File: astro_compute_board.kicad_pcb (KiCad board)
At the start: 4 copper layers, 66.4 x 66.2 mm, 81 parts, among them J1 SWD, J10 ADC_IO, J2 I2C1, J6 USB_B_Micro, J8 RaspberryHeader, J9 VINPUT, Q1 QM6015D, Q2 IRF540S, Q3 IRF540S, SW1 SW_SPDT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

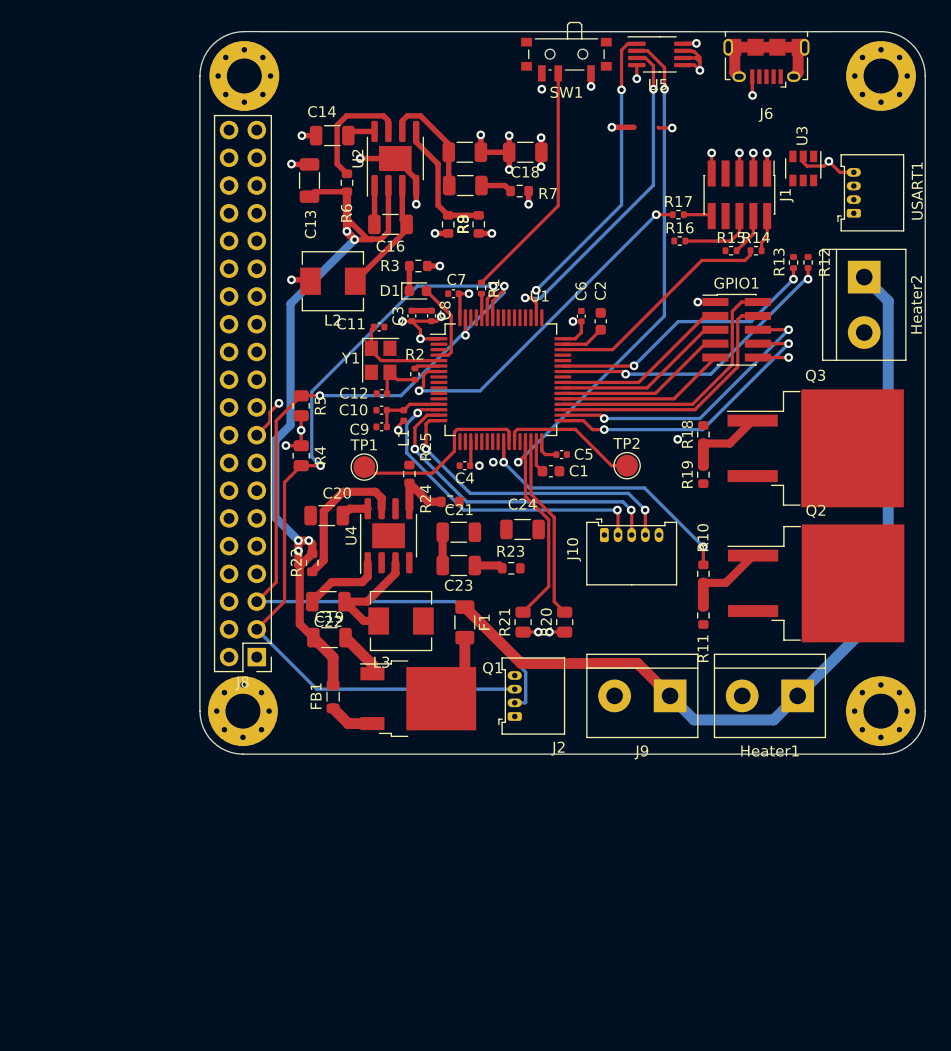
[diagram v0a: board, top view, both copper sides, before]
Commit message: JLCPCB Ready (but costly)
Contains many extender parts that make PCB expensive.
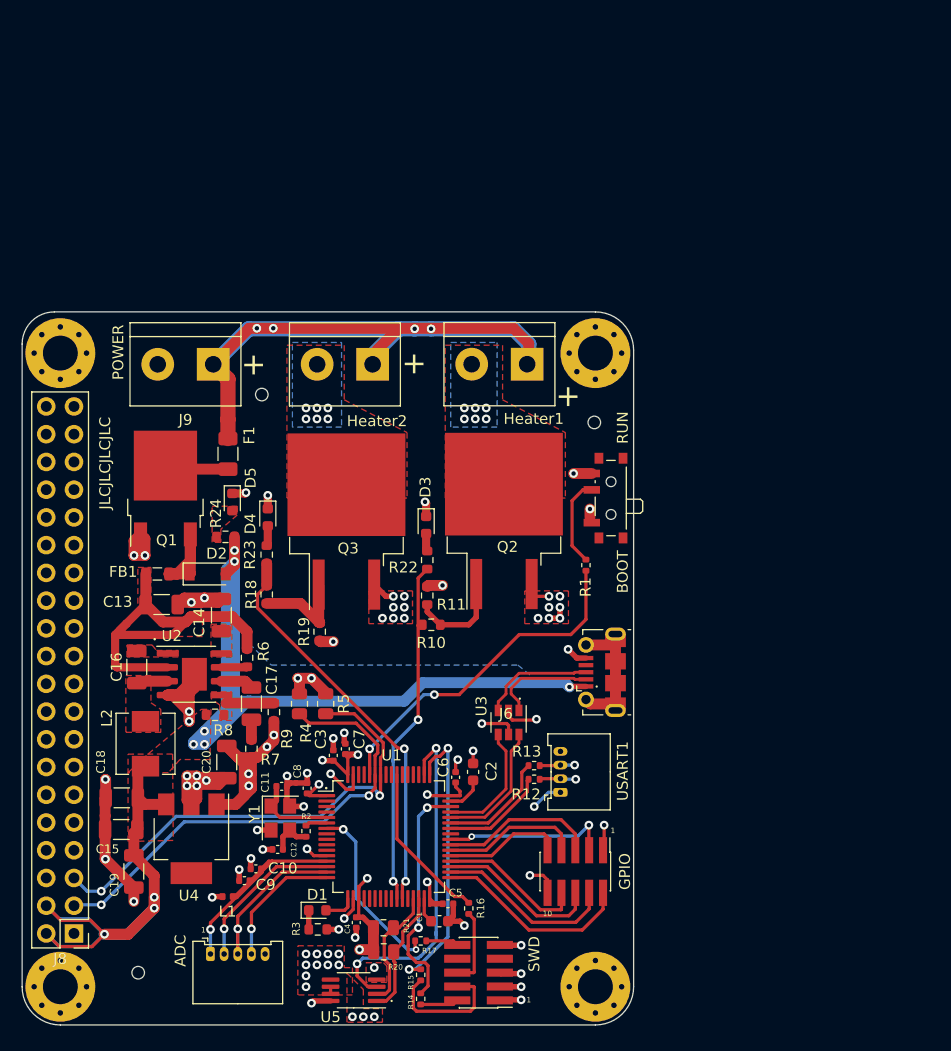
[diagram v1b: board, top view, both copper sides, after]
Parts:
- removed C21: Open, Capacitor_SMD:C_1206_3216Metric
- removed C22: 0.1u, Capacitor_SMD:C_1206_3216Metric
- removed C23: 2.2nF, Capacitor_SMD:C_1206_3216Metric
- removed C24: 22uF, Capacitor_SMD:C_1206_3216Metric
- removed GPIO1: GPIO_CONNECTOR, Connector_PinHeader_1.27mm:PinHeader_2x05_P1.27mm_Vertical_SMD
- removed J1: SWD, Connector_PinHeader_1.27mm:PinHeader_2x05_P1.27mm_Vertical_SMD
- removed J10: ADC_IO, Connector_Molex:Molex_PicoBlade_53048-0510_1x05_P1.25mm_Horizontal
- removed J2: I2C1, Connector_Molex:Molex_PicoBlade_53048-0410_1x04_P1.25mm_Horizontal
- removed L3: 6.8uH, Inductor_SMD:L_Sunlord_MWSA0518_5.4x5.2mm
- removed R25: 24k, Resistor_SMD:R_0603_1608Metric
- removed SW1: SW_SPDT, Button_Switch_SMD:SW_SPDT_PCM12
- removed TP1, TP2: TestPoint, TestPoint:TestPoint_Pad_D2.0mm
- added ADC: ADC_IO, Connector_Molex:Molex_PicoBlade_53048-0510_1x05_P1.25mm_Horizontal, F.Cu at (165.2, 151.7)
- added BOOT: SW_SPDT, Button_Switch_SMD:SW_SPDT_PCM12, F.Cu at (201.5, 109.9)
- added D2: B5817W-5819W, Diode_SMD:D_SOD-123, F.Cu at (164.9, 116.8)
- added D3: RED, LED_SMD:LED_0603_1608Metric, F.Cu at (184.9, 112.4)
- added D4: RED, LED_SMD:LED_0603_1608Metric, F.Cu at (170.4, 111.7)
- added D5: Green, LED_SMD:LED_0603_1608Metric, F.Cu at (167.2, 110.3)
- added GPIO: GPIO_CONNECTOR, Connector_PinHeader_1.27mm:PinHeader_2x05_P1.27mm_Vertical_SMD, F.Cu at (198.6, 144.1)
- added REF**: OSHW-Logo_11.4x12mm_SilkScreen, Symbol:OSHW-Logo_11.4x12mm_SilkScreen, B.Cu at (191.6, 110.5)
- added SWD: SWD, Connector_PinHeader_1.27mm:PinHeader_2x05_P1.27mm_Vertical_SMD, F.Cu at (189.7, 153.4)
- C15: value Open -> 22uF
- D1: value LED_Small -> BLUE
- J6: footprint Connector_USB:USB_Micro-B_Amphenol_10118194_Horizontal -> Connector_USB:USB_Micro-B_Molex-105017-0001
- R22: value 100k -> 1k
- R23: value 22k -> 1k
- R24: value 75k -> 1k
- R3: value 10k -> 2k
- R7: value 22k -> 33k
- R8: value 75k -> 62
- R9: value 24k -> 11.8
- U4: value RT7257BHZSP -> LM1117-3.3; footprint Package_SO:SOIC-8-1EP_3.9x4.9mm_P1.27mm_EP2.29x3mm -> Package_TO_SOT_SMD:SOT-223
- moved H3 112.3 mm to (151.4, 154.7)
- moved U5 90.2 mm to (178.3, 155.0), turned to 180 degrees
- moved H4 82.0 mm to (151.4, 96.6)
- moved R14 75.1 mm to (184.4, 155.8), turned to 270 degrees
- moved R15 72.1 mm to (184.4, 153.6), turned to 270 degrees
- moved R17 70.6 mm to (184.4, 150.4)
- moved C18 69.7 mm to (157.1, 137.3)
- moved C15 69.5 mm to (157.0, 140.2)
- moved R16 64.1 mm to (188.8, 147.5), turned to 270 degrees
- moved R3 61.4 mm to (175.0, 149.4)
- moved USART1 59.4 mm to (197.2, 136.8)
- moved J6 57.9 mm to (201.0, 125.8), turned to 90 degrees
- moved U3 57.5 mm to (192.5, 130.4)
- moved D1 57.5 mm to (175.0, 147.7)
- moved R7 56.7 mm to (168.9, 132.8), turned to 90 degrees
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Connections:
- C15 pad 1: GND -> +5V
- C15 pad 2: Net-(C15-Pad2) -> GND
- C17 pad 2: Net-(C15-Pad2) -> Net-(C17-Pad2)
- C18 pad 1: +3V3 -> +5V
- C19 pad 1: BUCK_VIN -> +5V
- C20 pad 1: Net-(C20-Pad1) -> +3V3
- L2 pad 2: +3V3 -> +5V
- R10 pad 2: PWM_B1 -> PWM_A2
- R18 pad 2: PWM_A1 -> PWM_B2
- R22 pad 1: Net-(R22-Pad1) -> Net-(D3-Pad2)
- R22 pad 2: BUCK_VIN -> PWM_A2
- R23 pad 1: GND -> Net-(D4-Pad2)
- R23 pad 2: Net-(C23-Pad1) -> PWM_B2
- R24 pad 1: Net-(R24-Pad1) -> Net-(D5-Pad2)
- R8 pad 2: +3V3 -> +5V
- U1 pad 24: PWM_A1 -> Net-(U1-Pad24)
- U1 pad 25: PWM_B1 -> Net-(U1-Pad25)
- U1 pad 33: GPIO_08 -> GPIO_05
- U1 pad 34: GPIO_07 -> GPIO_06
- U1 pad 35: GPIO_06 -> GPIO_07
- U1 pad 36: GPIO_05 -> GPIO_08
- U1 pad 4: LED_STATUS -> Net-(U1-Pad4)
- U2 pad 6: Net-(C15-Pad2) -> Net-(C17-Pad2)
- U4 pad 1: Net-(C22-Pad2) -> GND
- U4 pad 2: BUCK_VIN -> +3V3
- U4 pad 3: Net-(C22-Pad1) -> +5V
- U4 pad 4: GND -> (no net)
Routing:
- net +5V: track 0.00 -> 131.4 mm, vias 0 -> 9
- net GND: track 54.9 -> 126.7 mm, vias 21 -> 70
- net I2C2_SCL: track 64.7 -> 11.3 mm, vias 2 -> 0
- net BUCK_VIN: track 71.4 -> 35.3 mm, vias 5 -> 0
- net I2C1_SCL: track 78.0 -> 43.3 mm
- net I2C2_SDA: track 43.8 -> 11.6 mm, vias 2 -> 0
- net I2C1_SDA: track 75.2 -> 43.7 mm
- net BOOT0: track 2.21 -> 31.5 mm, vias 0 -> 2
- net SWCLCK: track 0.00 -> 26.5 mm, vias 0 -> 2
- net PWM_B1: track 26.0 -> 0.00 mm, vias 2 -> 0
- net PWM_B2: track 12.7 -> 37.1 mm, vias 0 -> 2
- net +3V3: track 45.3 -> 66.5 mm
- net USART1_TX: track 27.2 -> 9.87 mm, vias 2 -> 0
- net NRST: track 33.1 -> 16.6 mm
- net ADC1_IN2: track 28.3 -> 12.0 mm, vias 2 -> 1
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- added copper zone on In2.Cu, net +3V3
- added copper zone on B.Cu, net +5V
- added copper zone on F.Cu, net +5V
- added copper zone on F.Cu, net BUCK_VIN
- added copper zone on F.Cu, net GND
- added copper zone on In1.Cu, net GND
- added copper zone on F.Cu, net Net-(C14-Pad1)
- added copper zone on F.Cu, net Net-(C16-Pad1)
- added copper zone on F.Cu, net Net-(C16-Pad2)
- added copper zone on F.Cu, net Net-(D5-Pad2)
- added copper zone on B.Cu, net Net-(Heater1-Pad2)
- added copper zone on F.Cu, net Net-(Heater1-Pad2)
- added copper zone on B.Cu, net Net-(Heater2-Pad2)
- added copper zone on F.Cu, net Net-(Heater2-Pad2)
- added copper zone on F.Cu, net Net-(R8-Pad1)
- removed copper zone on In1.Cu, net +3V3
- removed copper zone on In2.Cu, net GND
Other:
- board size 66.4 x 66.2 mm -> 56 x 65.3 mm
- net class Default: trace_width 0.25 -> 0.3
- board text added: "+"
- board text added: "1"
- board text added: "10"
- board text added: "AstroCompute (Rev. 01)"
- board text added: "JLCJLCJLCJLC"
- board text added: "POWER"

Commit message: Rev2 - Out of Stock componets update (JLCPCB)
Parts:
- removed REF**: OSHW-Logo_11.4x12mm_SilkScreen, Symbol:OSHW-Logo_11.4x12mm_SilkScreen
- added R25: 800, Resistor_SMD:R_0603_1608Metric, F.Cu at (171.0, 132.8)
- C15, C17, C18: footprint Capacitor_SMD:C_1206_3216Metric -> Capacitor_SMD:C_0805_2012Metric
- C3: value 4uF -> 4.7uF
- R8: value 62 -> 62k
- R9: value 11.8 -> 11k
- U1: value STM32F405RGTx -> STM32F103R8T6
- moved R7 8.47 mm to (170.6, 124.6), turned to 270 degrees
- moved C17 1.53 mm to (169.6, 127.3), turned to 180 degrees
- moved R9 1.53 mm to (169.5, 129.6), turned to 180 degrees
- renumbered GPIO to GPIO1, SWD to J1, ADC to J10, BOOT to SW1
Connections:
- J8 pad 1: +3V3 -> Net-(J8-Pad1)
- J8 pad 17: +3V3 -> Net-(J8-Pad17)
- R9 pad 1: GND -> Net-(R25-Pad2)
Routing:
- net GND: track 126.7 -> 150.1 mm, vias 70 -> 71
- net +5V: track 131.4 -> 118.2 mm
- net Net-(R8-Pad1): track 4.38 -> 8.65 mm
- net Net-(R25-Pad2): track 0.00 -> 2.69 mm
- removed copper zone on B.Cu, net +5V
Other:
- board text added: "AstroCompute (Rev. 02)"
- board text removed: "AstroCompute (Rev. 01)"

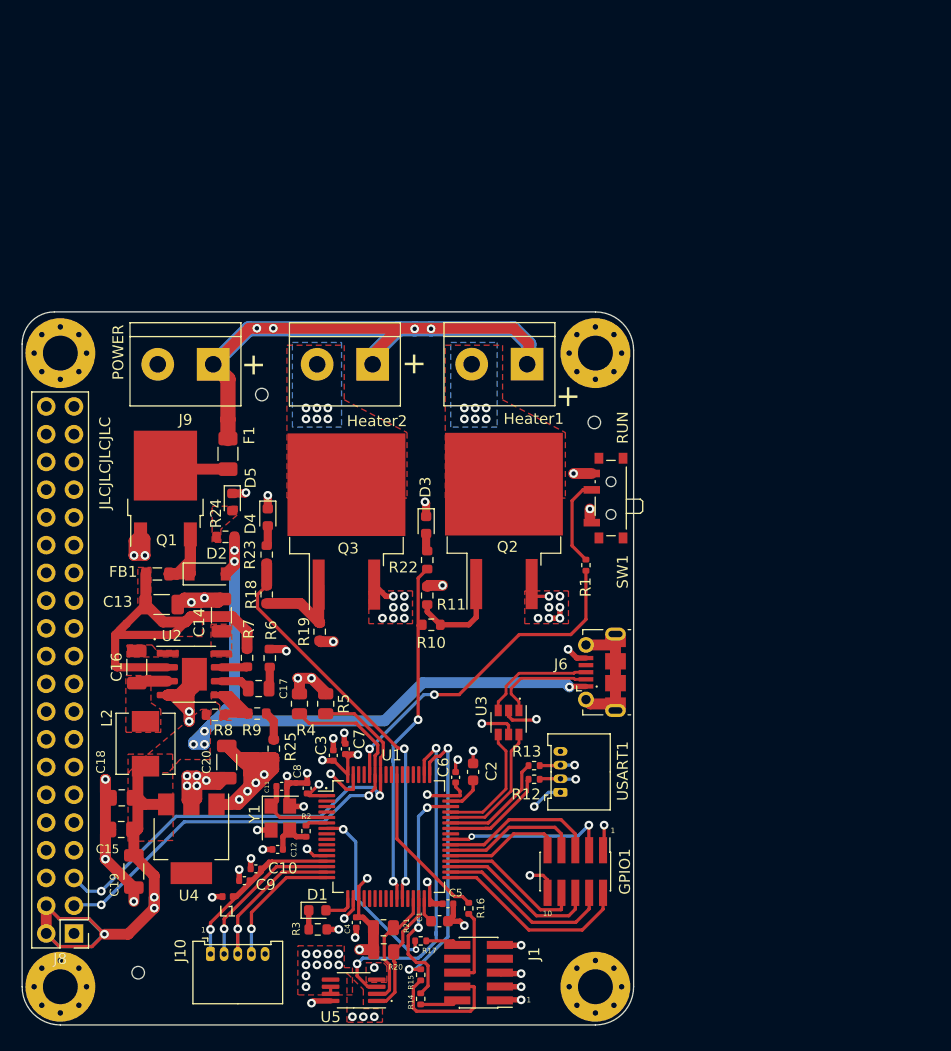
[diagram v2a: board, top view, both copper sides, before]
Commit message: Rev2.1 - Redesigned using Bulk Coverter and TH componets for easy testing
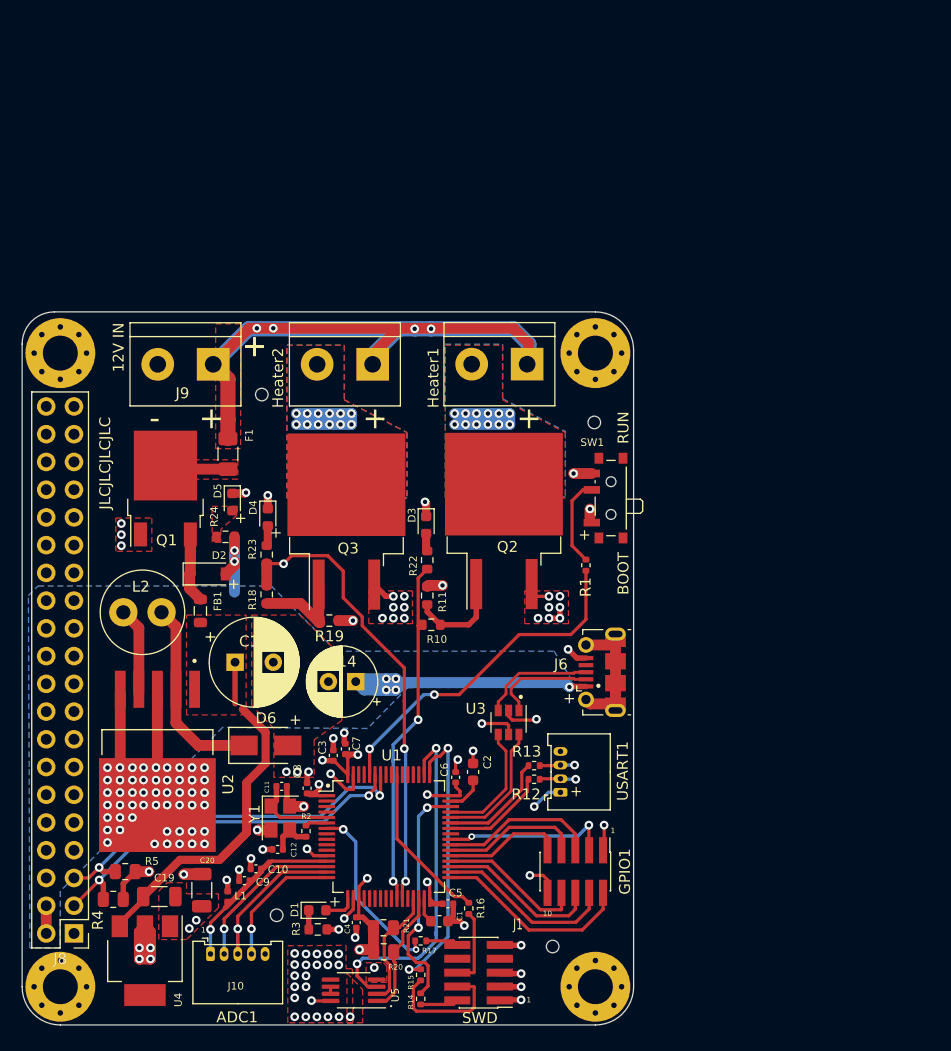
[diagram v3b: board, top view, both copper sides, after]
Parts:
- removed C15, C18: 22uF, Capacitor_SMD:C_0805_2012Metric
- removed C16: 0.1u, Capacitor_SMD:C_1206_3216Metric
- removed C17: 2.2nF, Capacitor_SMD:C_0805_2012Metric
- removed R25: 800, Resistor_SMD:R_0603_1608Metric
- removed R6: 100k, Resistor_SMD:R_0603_1608Metric
- removed R7: 33k, Resistor_SMD:R_0603_1608Metric
- removed R8: 62k, Resistor_SMD:R_0603_1608Metric
- removed R9: 11k, Resistor_SMD:R_0603_1608Metric
- added D6: SS54, Diode_SMD:D_SMA, F.Cu at (170.3, 132.6)
- C13: value 10uF -> 680uF; footprint Capacitor_SMD:C_1206_3216Metric -> Capacitor_THT:CP_Radial_D8.0mm_P3.50mm
- C14: value 0.1u -> 220uF; footprint Capacitor_SMD:C_1206_3216Metric -> Capacitor_THT:CP_Radial_D6.3mm_P2.50mm
- L2: value 6.8uH -> 33uH; footprint Inductor_SMD:L_Sunlord_MWSA0518_5.4x5.2mm -> Inductor_THT:L_Radial_D7.5mm_P3.50mm_Fastron_07P
- U2: value RT7257BHZSP -> LM2596SX-5.0_NOPB; footprint Package_SO:SOIC-8-1EP_3.9x4.9mm_P1.27mm_EP2.29x3mm -> lib:NOPB
- moved R4 24.7 mm to (156.3, 146.6), turned to 180 degrees
- moved R5 23.9 mm to (157.4, 144.1), turned to 180 degrees
- moved C14 13.7 mm to (178.5, 126.7), turned to 180 degrees
- moved U2 12.4 mm to (160.3, 138.0), turned to 270 degrees
- moved L2 12.1 mm to (160.7, 120.4), turned to 180 degrees
- moved C20 12.0 mm to (164.4, 145.8), turned to 270 degrees
- moved U4 11.9 mm to (159.2, 152.3)
- moved C13 8.55 mm to (167.4, 124.9)
- moved FB1 5.19 mm to (164.3, 120.2), turned to 90 degrees
- moved C19 3.28 mm to (160.5, 146.4), turned to 0 degrees
- moved R19 1.35 mm to (176.1, 121.1), turned to 180 degrees
- turned L1 to 270 degrees
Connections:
- C14 pad 1: Net-(C14-Pad1) -> +5V
- C19 pad 1: +5V -> BUCK_VIN
- L2 pad 1: Net-(C16-Pad1) -> Net-(D6-Pad1)
- U2 pad 1: Net-(C16-Pad2) -> BUCK_VIN
- U2 pad 2: BUCK_VIN -> Net-(D6-Pad1)
- U2 pad 3: Net-(C16-Pad1) -> GND
- U2 pad 4: GND -> +5V
- U2 pad 5: Net-(R8-Pad1) -> GND
- U2 pad 6: Net-(C17-Pad2) -> GND
- U4 pad 3: +5V -> BUCK_VIN
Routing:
- net +5V: track 118.2 -> 51.3 mm, vias 9 -> 7
- net GND: track 150.1 -> 83.5 mm, vias 71 -> 122
- net Net-(D6-Pad1): track 0.00 -> 17.8 mm
- net Net-(Heater2-Pad2): track 0.00 -> 11.1 mm, vias 6 -> 12
- net Net-(Heater1-Pad2): track 0.00 -> 11.1 mm, vias 6 -> 12
- net Net-(R8-Pad1): track 8.65 -> 0.00 mm
- net I2C1_SDA: track 43.7 -> 35.4 mm
- net I2C1_SCL: track 43.3 -> 35.4 mm
- net PWM_B2: track 37.1 -> 42.4 mm, vias 2 -> 3
- net BUCK_VIN: track 35.3 -> 40.1 mm
- net Net-(C16-Pad1): track 2.87 -> 0.00 mm
- net Net-(C17-Pad2): track 2.74 -> 0.00 mm
- net Net-(R25-Pad2): track 2.69 -> 0.00 mm
- net Net-(R6-Pad1): track 2.37 -> 0.00 mm
- net Net-(C17-Pad1): track 2.00 -> 0.00 mm
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- added copper zone on F.Cu, net +12V
- added copper zone on B.Cu, net +5V
- added copper zone on F.Cu, net Net-(F1-Pad2)
- removed copper zone on F.Cu, net +5V
- removed copper zone on F.Cu, net Net-(C14-Pad1)
- removed copper zone on F.Cu, net Net-(C16-Pad1)
- removed copper zone on F.Cu, net Net-(C16-Pad2)
- removed copper zone on F.Cu, net Net-(R8-Pad1)
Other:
- outline, holes or cut-outs redrawn
- board text added: "-"
- board text added: "12V IN"
- board text added: "ADC1"
- board text added: "BOOT"
- board text added: "SWD"
- board text removed: "POWER"
